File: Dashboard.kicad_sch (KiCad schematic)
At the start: 11 parts

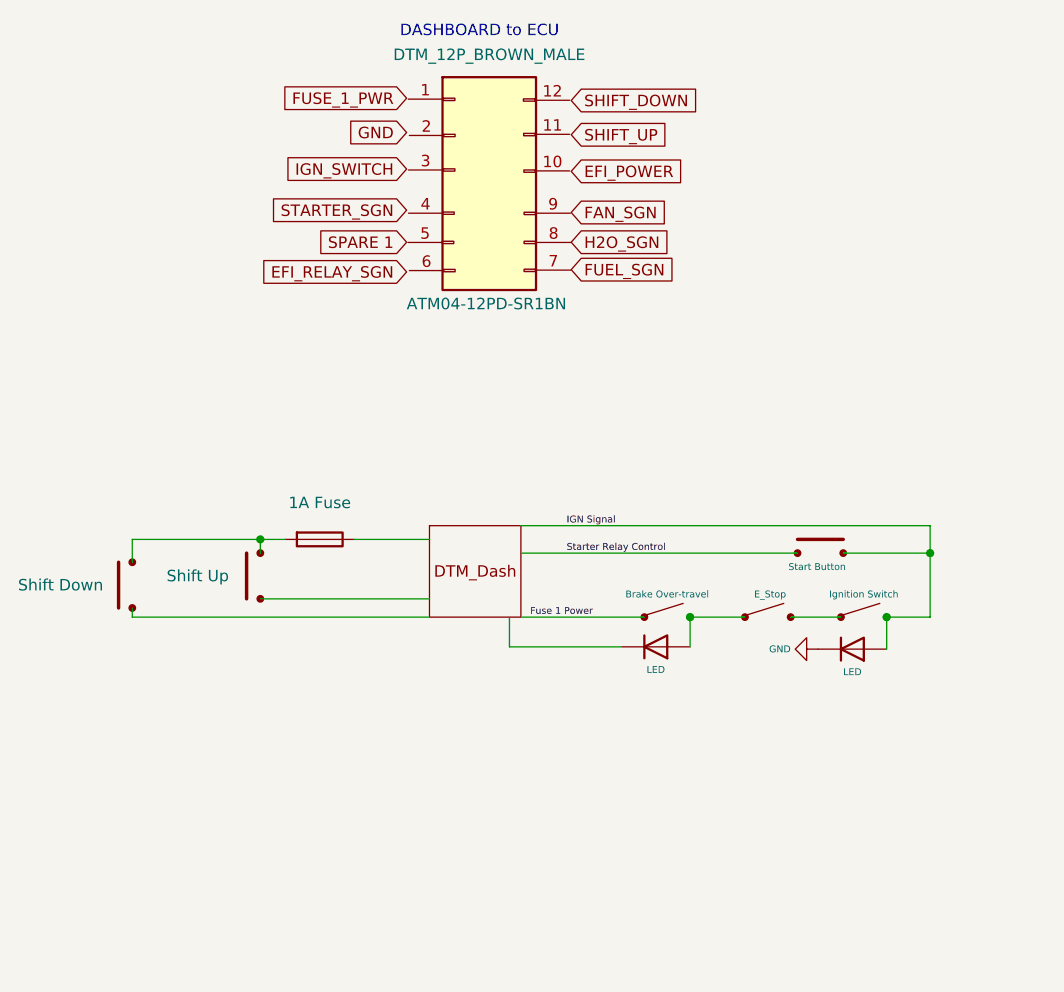
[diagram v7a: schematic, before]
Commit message: Connector Numbers 1
Added Numbers to all of the connectors that were numbered and in KiCad so far
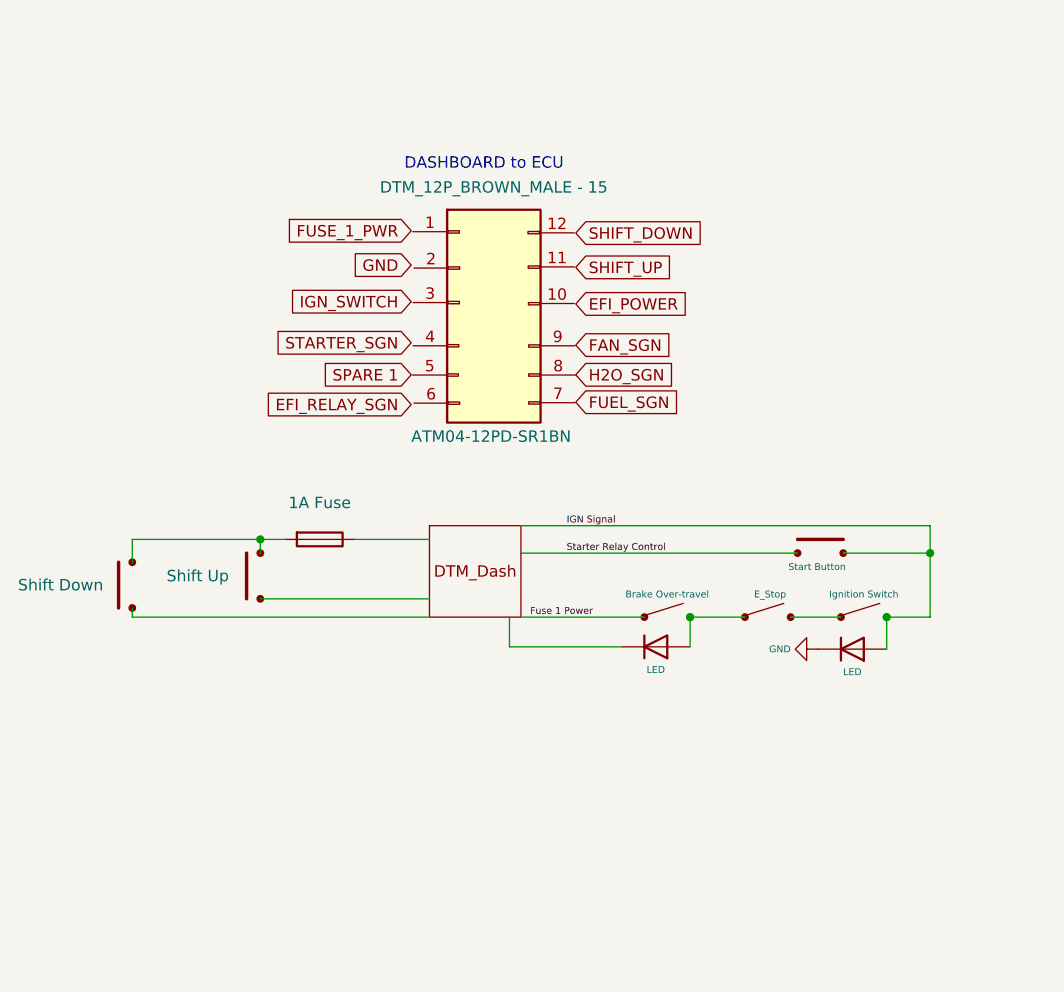
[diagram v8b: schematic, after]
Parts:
- U?: value DTM_12P_BROWN_MALE -> DTM_12P_BROWN_MALE - 15
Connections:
- new net: D?.1 (A), U?., U?.
- new net: F?.2, U?., U?.
- now unconnected: U?., U?.
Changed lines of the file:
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@@
     (stroke (width 0) (type default) (color 0 0 0 0))
   )
-  (text "DASHBOARD to ECU" (at 131.064 41.148 0)
+  (text "DASHBOARD to ECU" (at 131.572 55.88 0)
     (effects (font (size 1.27 1.27)) (justify left bottom))
   )
@@
     (effects (font (size 0.762 0.762)) (justify left bottom))
   )
-  (global_label "EFI_RELAY_SGN" (shape input) (at 131.826 67.056 180) (fields_autoplaced)
-    (effects (font (size 1.27 1.27)) (justify right))
-    (property "Intersheet References" "${INTERSHEET_REFS}" (id 0) (at 115.201 66.9766 0)
-      (effects (font (size 1.27 1.27)) (justify right) hide)
-    )
-  )
-  (global_label "EFI_POWER" (shape input) (at 150.114 55.88 0) (fields_autoplaced)
-    (effects (font (size 1.27 1.27)) (justify left))
-    (property "Intersheet References" "${INTERSHEET_REFS}" (id 0) (at 162.8081 55.8006 0)
-      (effects (font (size 1.27 1.27)) (justify left) hide)
-    )
-  )
-  (global_label "SHIFT_DOWN" (shape input) (at 150.114 48.006 0) (fields_autoplaced)
-    (effects (font (size 1.27 1.27)) (justify left))
-    (property "Intersheet References" "${INTERSHEET_REFS}" (id 0) (at 164.0781 47.9266 0)
-      (effects (font (size 1.27 1.27)) (justify left) hide)
-    )
-  )
-  (global_label "SHIFT_UP" (shape input) (at 150.114 51.816 0) (fields_autoplaced)
-    (effects (font (size 1.27 1.27)) (justify left))
-    (property "Intersheet References" "${INTERSHEET_REFS}" (id 0) (at 161.2961 51.7366 0)
-      (effects (font (size 1.27 1.27)) (justify left) hide)
-    )
-  )
-  (global_label "IGN_SWITCH" (shape input) (at 131.826 55.626 180) (fields_autoplaced)
-    (effects (font (size 1.27 1.27)) (justify right))
-    (property "Intersheet References" "${INTERSHEET_REFS}" (id 0) (at 118.4062 55.5466 0)
-      (effects (font (size 1.27 1.27)) (justify right) hide)
-    )
-  )
-  (global_label "FAN_SGN" (shape input) (at 150.114 60.452 0) (fields_autoplaced)
-    (effects (font (size 1.27 1.27)) (justify left))
-    (property "Intersheet References" "${INTERSHEET_REFS}" (id 0) (at 160.8123 60.3726 0)
-      (effects (font (size 1.27 1.27)) (justify left) hide)
-    )
-  )
-  (global_label "SPARE 1" (shape input) (at 131.826 63.754 180) (fields_autoplaced)
-    (effects (font (size 1.27 1.27)) (justify right))
-    (property "Intersheet References" "${INTERSHEET_REFS}" (id 0) (at 121.2486 63.6746 0)
-      (effects (font (size 1.27 1.27)) (justify right) hide)
-    )
-  )
-  (global_label "H2O_SGN" (shape input) (at 150.114 63.754 0) (fields_autoplaced)
-    (effects (font (size 1.27 1.27)) (justify left))
-    (property "Intersheet References" "${INTERSHEET_REFS}" (id 0) (at 161.1752 63.6746 0)
-      (effects (font (size 1.27 1.27)) (justify left) hide)
-    )
-  )
-  (global_label "FUSE_1_PWR" (shape input) (at 131.826 47.752 180) (fields_autoplaced)
-    (effects (font (size 1.27 1.27)) (justify right))
-    (property "Intersheet References" "${INTERSHEET_REFS}" (id 0) (at 117.4991 47.6726 0)
-      (effects (font (size 1.27 1.27)) (justify right) hide)
-    )
-  )
-  (global_label "STARTER_SGN" (shape input) (at 131.826 60.198 180) (fields_autoplaced)
-    (effects (font (size 1.27 1.27)) (justify right))
-    (property "Intersheet References" "${INTERSHEET_REFS}" (id 0) (at 116.7129 60.1186 0)
-      (effects (font (size 1.27 1.27)) (justify right) hide)
-    )
-  )
-  (global_label "FUEL_SGN" (shape input) (at 150.114 66.802 0) (fields_autoplaced)
-    (effects (font (size 1.27 1.27)) (justify left))
-    (property "Intersheet References" "${INTERSHEET_REFS}" (id 0) (at 161.9009 66.7226 0)
-      (effects (font (size 1.27 1.27)) (justify left) hide)
-    )
-  )
-  (global_label "GND" (shape input) (at 131.826 51.562 180) (fields_autoplaced)
-    (effects (font (size 1.27 1.27)) (justify right))
-    (property "Intersheet References" "${INTERSHEET_REFS}" (id 0) (at 125.5424 51.4826 0)
+  (global_label "EFI_RELAY_SGN" (shape input) (at 132.334 81.788 180) (fields_autoplaced)
+    (effects (font (size 1.27 1.27)) (justify right))
+    (property "Intersheet References" "${INTERSHEET_REFS}" (id 0) (at 115.709 81.7086 0)
+      (effects (font (size 1.27 1.27)) (justify right) hide)
+    )
+  )
+  (global_label "EFI_POWER" (shape input) (at 150.622 70.612 0) (fields_autoplaced)
+    (effects (font (size 1.27 1.27)) (justify left))
+    (property "Intersheet References" "${INTERSHEET_REFS}" (id 0) (at 163.3161 70.5326 0)
+      (effects (font (size 1.27 1.27)) (justify left) hide)
+    )
+  )
+  (global_label "SHIFT_DOWN" (shape input) (at 150.622 62.738 0) (fields_autoplaced)
+    (effects (font (size 1.27 1.27)) (justify left))
+    (property "Intersheet References" "${INTERSHEET_REFS}" (id 0) (at 164.5861 62.6586 0)
+      (effects (font (size 1.27 1.27)) (justify left) hide)
+    )
+  )
+  (global_label "SHIFT_UP" (shape input) (at 150.622 66.548 0) (fields_autoplaced)
+    (effects (font (size 1.27 1.27)) (justify left))
+    (property "Intersheet References" "${INTERSHEET_REFS}" (id 0) (at 161.8041 66.4686 0)
+      (effects (font (size 1.27 1.27)) (justify left) hide)
+    )
+  )
+  (global_label "IGN_SWITCH" (shape input) (at 132.334 70.358 180) (fields_autoplaced)
+    (effects (font (size 1.27 1.27)) (justify right))
+    (property "Intersheet References" "${INTERSHEET_REFS}" (id 0) (at 118.9142 70.2786 0)
+      (effects (font (size 1.27 1.27)) (justify right) hide)
+    )
+  )
+  (global_label "FAN_SGN" (shape input) (at 150.622 75.184 0) (fields_autoplaced)
+    (effects (font (size 1.27 1.27)) (justify left))
+    (property "Intersheet References" "${INTERSHEET_REFS}" (id 0) (at 161.3203 75.1046 0)
+      (effects (font (size 1.27 1.27)) (justify left) hide)
+    )
+  )
+  (global_label "SPARE 1" (shape input) (at 132.334 78.486 180) (fields_autoplaced)
+    (effects (font (size 1.27 1.27)) (justify right))
+    (property "Intersheet References" "${INTERSHEET_REFS}" (id 0) (at 121.7566 78.4066 0)
+      (effects (font (size 1.27 1.27)) (justify right) hide)
+    )
+  )
+  (global_label "H2O_SGN" (shape input) (at 150.622 78.486 0) (fields_autoplaced)
+    (effects (font (size 1.27 1.27)) (justify left))
+    (property "Intersheet References" "${INTERSHEET_REFS}" (id 0) (at 161.6832 78.4066 0)
+      (effects (font (size 1.27 1.27)) (justify left) hide)
+    )
+  )
+  (global_label "FUSE_1_PWR" (shape input) (at 132.334 62.484 180) (fields_autoplaced)
+    (effects (font (size 1.27 1.27)) (justify right))
+    (property "Intersheet References" "${INTERSHEET_REFS}" (id 0) (at 118.0071 62.4046 0)
+      (effects (font (size 1.27 1.27)) (justify right) hide)
+    )
+  )
+  (global_label "STARTER_SGN" (shape input) (at 132.334 74.93 180) (fields_autoplaced)
+    (effects (font (size 1.27 1.27)) (justify right))
+    (property "Intersheet References" "${INTERSHEET_REFS}" (id 0) (at 117.2209 74.8506 0)
+      (effects (font (size 1.27 1.27)) (justify right) hide)
+    )
+  )
+  (global_label "FUEL_SGN" (shape input) (at 150.622 81.534 0) (fields_autoplaced)
+    (effects (font (size 1.27 1.27)) (justify left))
+    (property "Intersheet References" "${INTERSHEET_REFS}" (id 0) (at 162.4089 81.4546 0)
+      (effects (font (size 1.27 1.27)) (justify left) hide)
+    )
+  )
+  (global_label "GND" (shape input) (at 132.334 66.294 180) (fields_autoplaced)
+    (effects (font (size 1.27 1.27)) (justify right))
+    (property "Intersheet References" "${INTERSHEET_REFS}" (id 0) (at 126.0504 66.2146 0)
       (effects (font (size 1.27 1.27)) (justify right) hide)
     )
@@
     (pin "2")
   )
-  (symbol (lib_id "SCR23 Library:DTM04-12pb") (at 140.716 58.166 0) (unit 1)
-    (in_bom yes) (on_board yes)
-    (property "Reference" "U?" (id 0) (at 141.0081 40.386 0)
-      (effects (font (size 1.27 1.27)) hide)
-    )
-    (property "Value" "DTM_12P_BROWN_MALE" (id 1) (at 141.0081 42.926 0))
-    (property "Footprint" "" (id 2) (at 140.716 68.326 0)
-      (effects (font (size 1.27 1.27)) hide)
-    )
-    (property "Datasheet" "" (id 3) (at 140.716 68.326 0)
-      (effects (font (size 1.27 1.27)) hide)
-    )
-    (property "Part #" "ATM04-12PD-SR1BN" (id 4) (at 140.716 70.612 0))
+  (symbol (lib_id "SCR23 Library:DTM04-12pb") (at 141.224 72.898 0) (unit 1)
+    (in_bom yes) (on_board yes)
+    (property "Reference" "U?" (id 0) (at 141.5161 55.118 0)
+      (effects (font (size 1.27 1.27)) hide)
+    )
+    (property "Value" "DTM_12P_BROWN_MALE - 15" (id 1) (at 141.5161 57.658 0))
+    (property "Footprint" "" (id 2) (at 141.224 83.058 0)
+      (effects (font (size 1.27 1.27)) hide)
+    )
+    (property "Datasheet" "" (id 3) (at 141.224 83.058 0)
+      (effects (font (size 1.27 1.27)) hide)
+    )
+    (property "Part #" "ATM04-12PD-SR1BN" (id 4) (at 141.224 85.344 0))
     (pin "1")
     (pin "10")
